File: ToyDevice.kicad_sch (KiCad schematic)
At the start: 45 parts, among them J1 USB_C_Receptacle_USB2.0, J2 Conn_ARM_JTAG_SWD_10, SW1 SW_SPDT, SW2 SW_Push, SW3 SW_Push, SW4 SW_Push, SW5 SW_Push, U1 LP5907MFX-3.3, U2 STM32F070F6Px, Y1 8Mhz Crystal

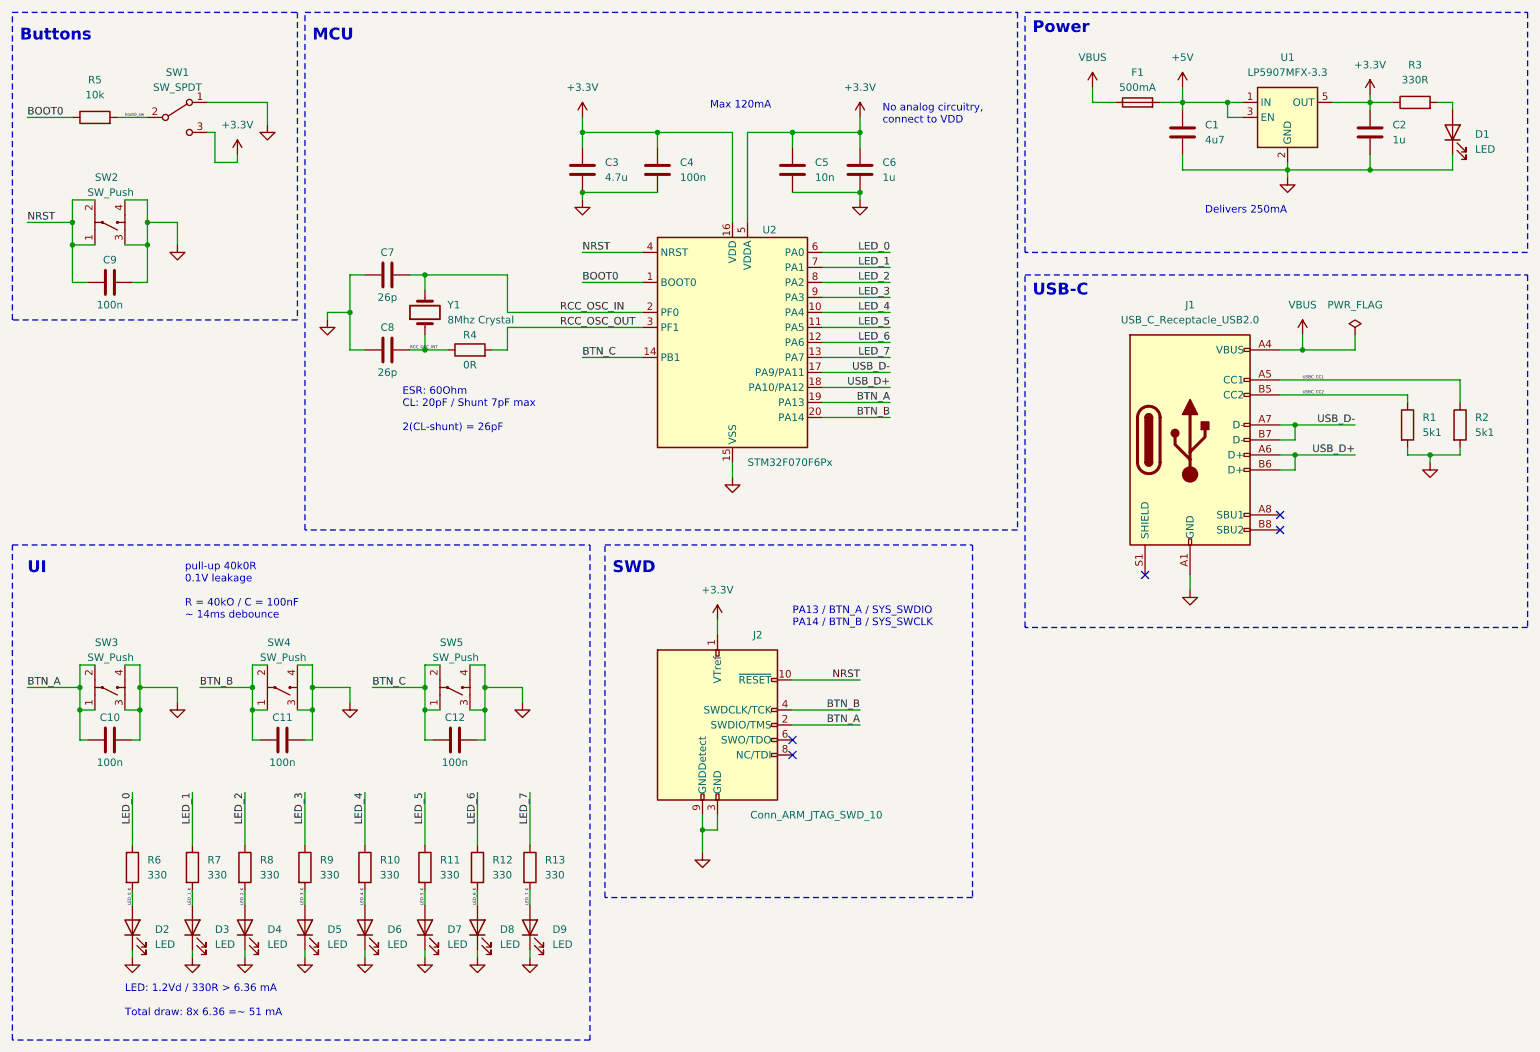
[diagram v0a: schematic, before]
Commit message: Add all part number
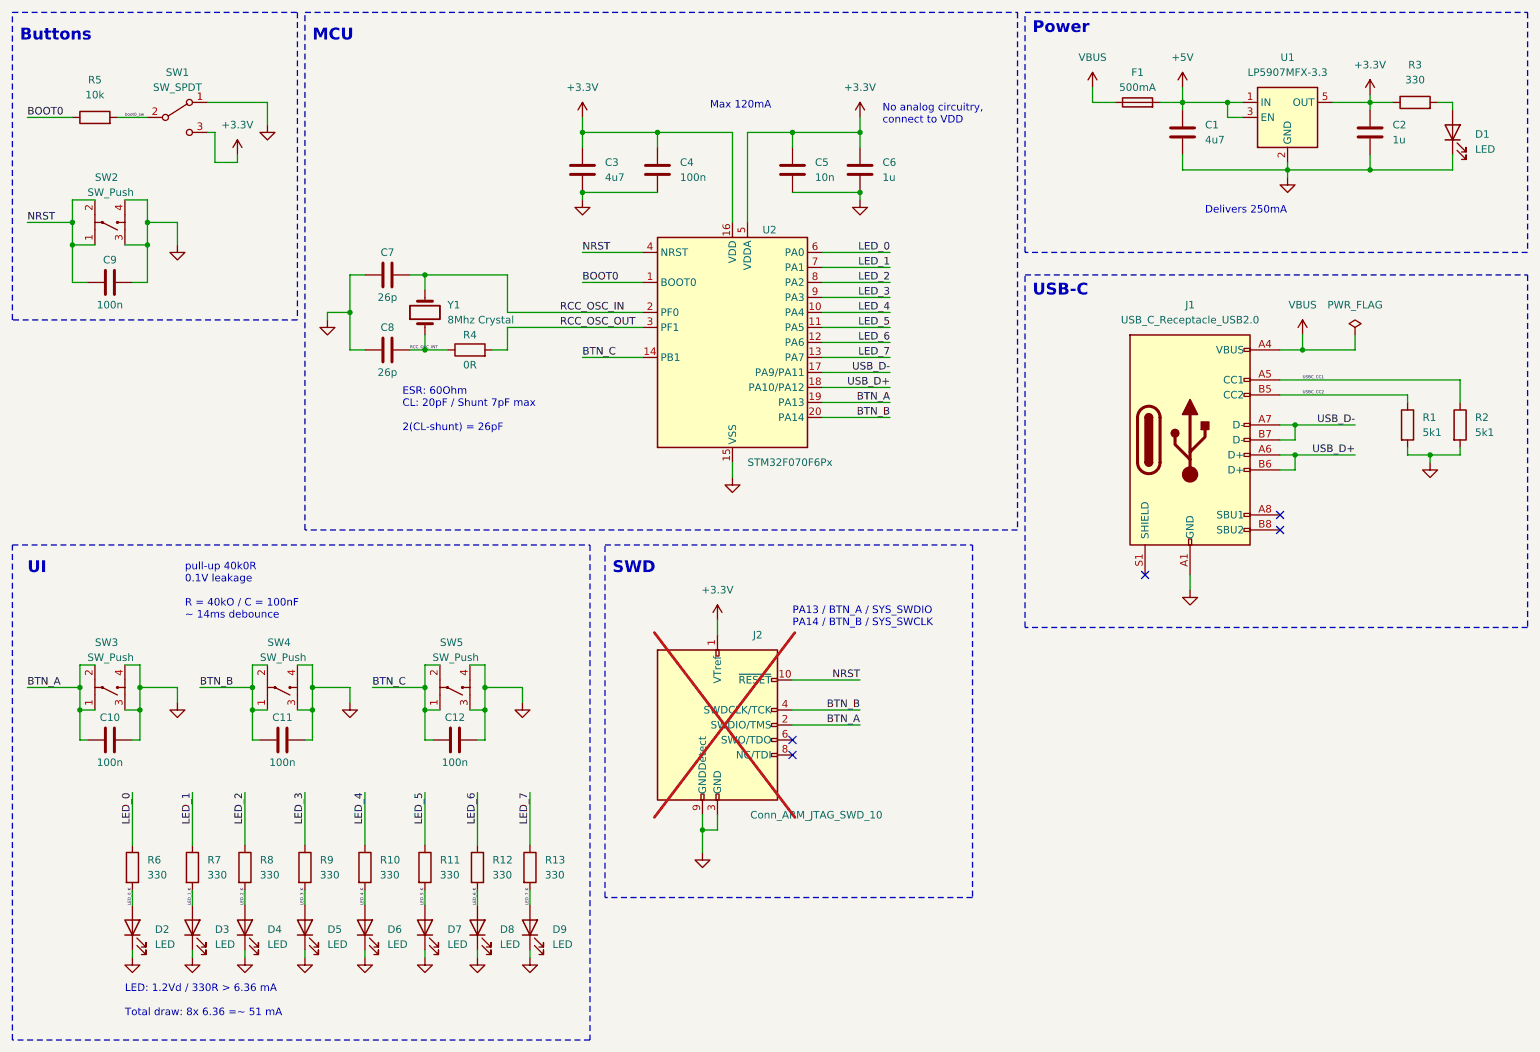
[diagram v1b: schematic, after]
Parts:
- C1: LCSC (none) -> C368809; Mfr Part (none) -> CL05A475KP5NRNC
- C10, C11, C12, C2, C4, C6, C9: LCSC (none) -> C107372; Mfr Part (none) -> CL05A105KQ5NNNC
- C3: value 4.7u -> 4u7; LCSC (none) -> C368809; Mfr Part (none) -> CL05A475KP5NRNC
- C5: LCSC (none) -> C1518210; Mfr Part (none) -> GRM1555CYA103JE01D
- C7, C8: footprint Capacitor_SMD:C_0402_1005Metric -> Capacitor_SMD:C_0603_1608Metric; LCSC (none) -> C5177174; Mfr Part (none) -> CS1608C0G220J500NRB
- D1, D2, D3, D4, D5, D6, D7, D8, D9: LCSC (none) -> C138542; Mfr Part (none) -> BL-HKC36P-TRB
- F1: LCSC (none) -> C136320; Mfr Part (none) -> JFC0402-0500FS
- J1: LCSC (none) -> C3001297; Mfr Part (none) -> GT-USB-7010EN
- J2: now not fitted
- R1, R2: LCSC (none) -> C350580; Mfr Part (none) -> RC-02W512FT
- R10, R11, R12, R13, R6, R7, R8, R9: LCSC (none) -> C5139567; Mfr Part (none) -> RAT023300FTH
- R3: value 330R -> 330; LCSC (none) -> C5139567; Mfr Part (none) -> RAT023300FTH
- R4: LCSC (none) -> C380743; Mfr Part (none) -> SY0402JN0RP
- R5: LCSC (none) -> C308028; Mfr Part (none) -> MCR01MZPJ103
- U1: LCSC (none) -> C80670; Mfr Part (none) -> LP5907MFX-3.3/NOPB
- U2: LCSC (none) -> C86951; Mfr Part (none) -> STM32F070F6P6
- Y1: LCSC (none) -> C240959; Mfr Part (none) -> 49MD-8.000-20-20-20/A

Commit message: Changed USB-C connector
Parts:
- removed R4: 0R, Resistor_SMD:R_0402_1005Metric, symbol Device:R
- C1, C3: LCSC C368809 -> C5173643; Mfr Part CL05A475KP5NRNC -> 0402X475K6R3CT
- C2, C6: LCSC C107372 -> C913490; Mfr Part CL05A105KQ5NNNC -> GRM155R70J105MA12D
- C7, C8: value 26p -> 15p; footprint Capacitor_SMD:C_0603_1608Metric -> Capacitor_SMD:C_0402_1005Metric; LCSC C5177174 -> C386131; Mfr Part CS1608C0G220J500NRB -> UMK105CG220JV-F
- D1, D2, D3, D4, D5, D6, D7, D8, D9: LCSC C138542 -> C72038; Mfr Part BL-HKC36P-TRB -> 19-213/Y2C-CQ2R2L/3T(CY)
- J1: footprint Connector_USB:USB_C_Receptacle_G-Switch_GT-USB-7010ASV -> Hugo_Custom:SHOU-HAN-TYPE-C-16PFS-2J-H7-45-IPX8; LCSC C3001297 -> C3020050; Mfr Part GT-USB-7010EN -> TYPE-C 16PFS 2J-H7.45 IPX8
- R1, R2: LCSC C350580 -> C2692894; Mfr Part RC-02W512FT -> PTFR0402B5K11P9
- R10, R11, R12, R13, R3, R6, R7, R8, R9: value 330 -> 330R
- Y1: footprint Crystal:Crystal_SMD_HC49-SD -> Crystal:Crystal_SMD_3225-4Pin_3.2x2.5mm; symbol Device:Crystal -> Device:Crystal_GND24; LCSC C240959 -> C479191; Mfr Part 49MD-8.000-20-20-20/A -> S32080001010500
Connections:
- net RCC_OSC_INT is gone; now on net RCC_OSC_OUT: C8.2, Y1.1
- net GND: now also Y1.2, Y1.4
- net RCC_OSC_IN: now also Y1.3; no longer Y1.2
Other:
- note added: "ESR: 60Ohm CL: 10pF / Shunt 7pF max - avg 3pF 2(CL-shunt) = 14pF"
- note removed: "ESR: 60Ohm CL: 20pF / Shunt 7pF max 2(CL-shunt) = 26pF"
- moved on the sheet: C7, C8

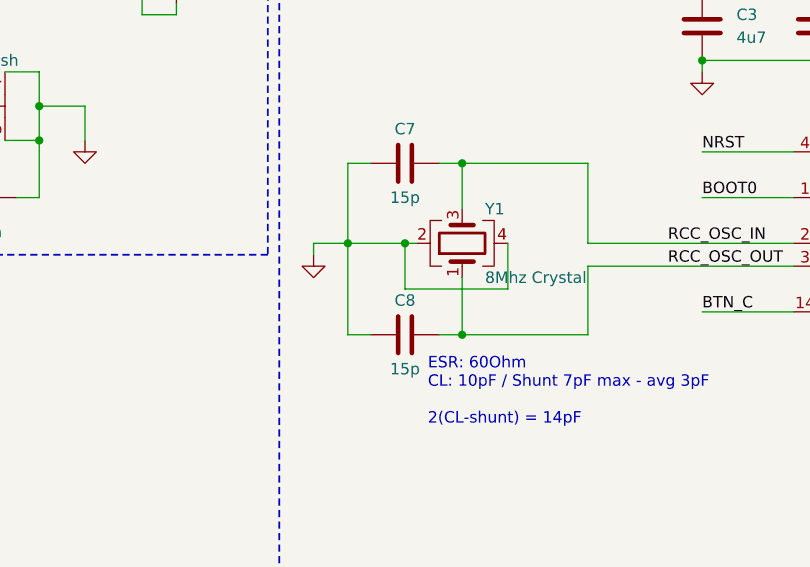
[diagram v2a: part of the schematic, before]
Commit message: Change crystal capacitor to available type
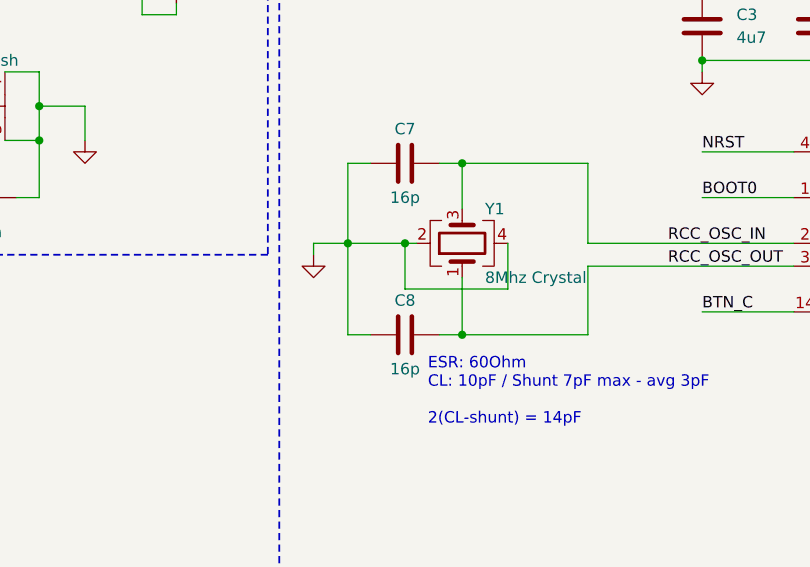
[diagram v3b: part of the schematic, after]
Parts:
- C7, C8: value 15p -> 16p; LCSC C386131 -> C513591; Mfr Part UMK105CG220JV-F -> CC0402GRNPO9BN160
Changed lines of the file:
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@@
       (effects (font (size 1.27 1.27)))
     )
-    (property "Value" "15p" (at 77.47 78.74 90)
+    (property "Value" "16p" (at 77.47 78.74 90)
       (effects (font (size 1.27 1.27)))
     )
@@
       (effects (font (size 1.27 1.27)) hide)
     )
-    (property "LCSC" "C386131" (at 77.47 74.93 0)
-      (effects (font (size 1.27 1.27)) hide)
-    )
-    (property "Mfr Part" "UMK105CG220JV-F" (at 77.47 74.93 0)
+    (property "LCSC" "C513591" (at 77.47 74.93 0)
+      (effects (font (size 1.27 1.27)) hide)
+    )
+    (property "Mfr Part" "CC0402GRNPO9BN160" (at 77.47 74.93 0)
       (effects (font (size 1.27 1.27)) hide)
     )
@@
       (effects (font (size 1.27 1.27)))
     )
-    (property "Value" "15p" (at 77.47 59.69 90)
+    (property "Value" "16p" (at 77.47 59.69 90)
       (effects (font (size 1.27 1.27)))
     )
@@
       (effects (font (size 1.27 1.27)) hide)
     )
-    (property "LCSC" "C386131" (at 77.47 55.88 0)
-      (effects (font (size 1.27 1.27)) hide)
-    )
-    (property "Mfr Part" "UMK105CG220JV-F" (at 77.47 55.88 0)
-      (effects (font (size 1.27 1.27)) hide)
-    )
+    (property "LCSC" "C513591" (at 77.47 55.88 0)
+      (effects (font (size 1.27 1.27)) hide)
+    )
+    (property "Mfr Part" "CC0402GRNPO9BN160" (at 77.47 55.88 0)
+      (effects (font (size 1.27 1.27)) hide)
+    )
